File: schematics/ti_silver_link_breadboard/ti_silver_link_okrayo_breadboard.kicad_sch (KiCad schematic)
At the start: 35 parts, among them P1 USB_B, U1 24LC256, U2 MCP17003302E, U3 TUSB3410, U4A PN2222A, U4B PN2222A, Y1 12MHz

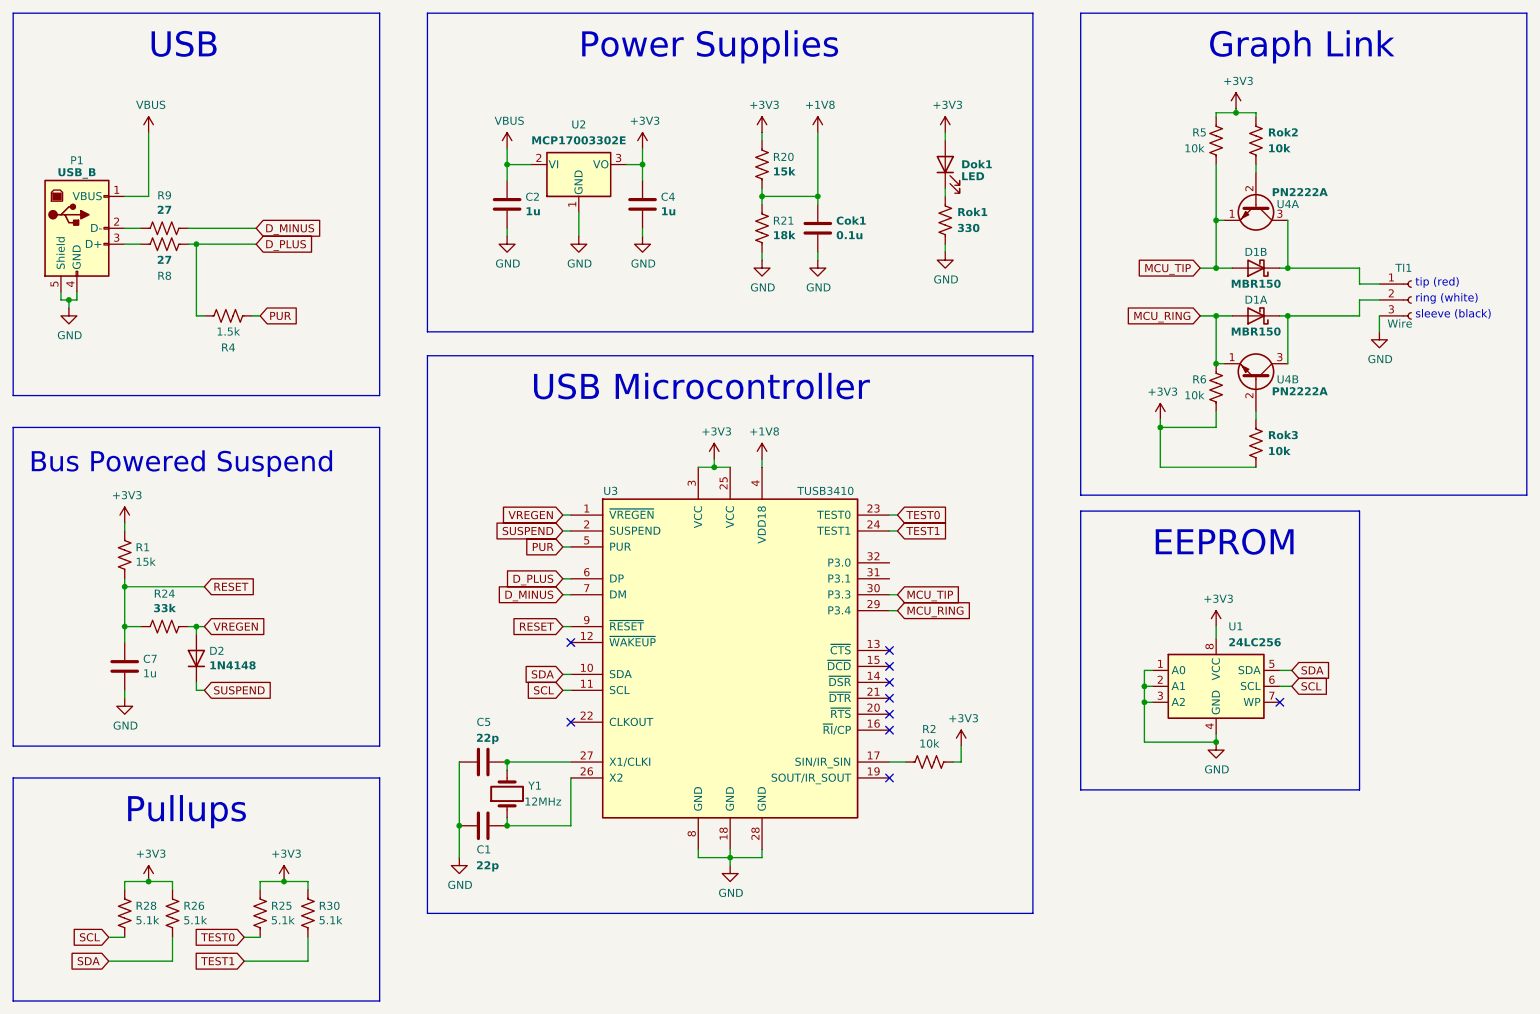
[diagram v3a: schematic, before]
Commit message: Move I2C and TEST pullups near their respective devices
 - Move I2C pullups near EEPROM
 - Move TEST pullups near TUSB3410
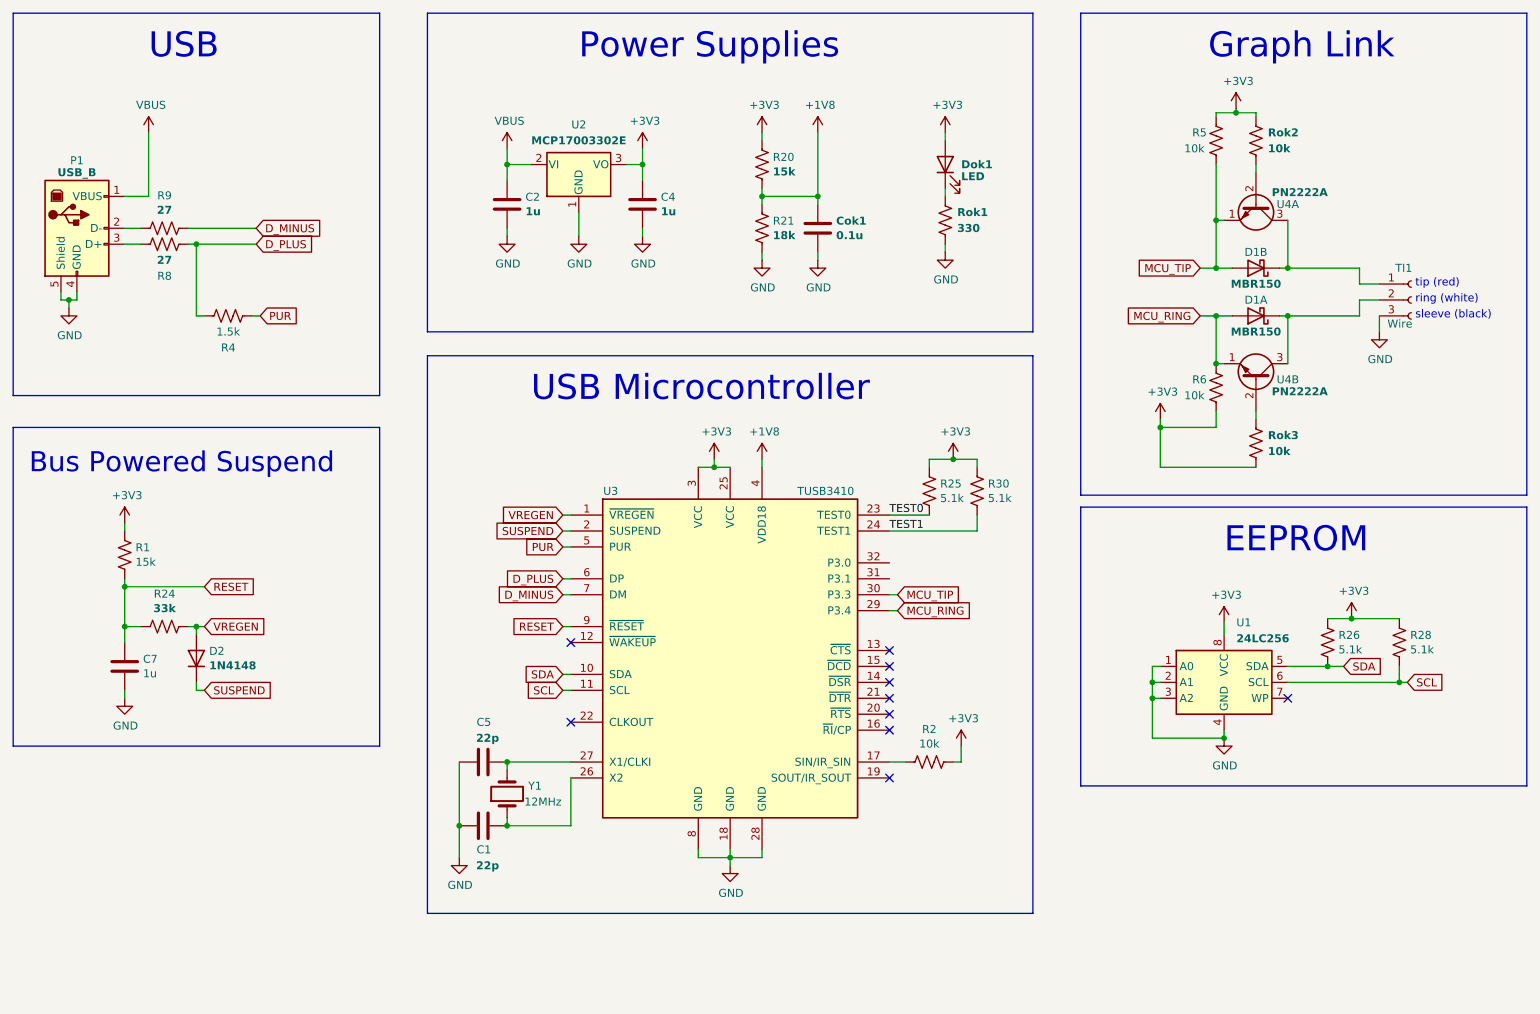
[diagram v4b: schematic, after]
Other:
- note removed: "Pullups"
- moved on the sheet: R25, R26, R28, R30, U1
